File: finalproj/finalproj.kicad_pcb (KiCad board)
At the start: 2 copper layers, 99.2 x 99.6 mm, 44 parts, among them J10 MotorA Out, J11 MotorB Out, J5 Stepper_Motor_Controller, J7 LIDAR_Connector, J9 RPI_UART_Conn, U1 LM1085-12, U2 LM1085-12, U3 LM1085-5.0, U4 LM1085-3.3, U5 L298N

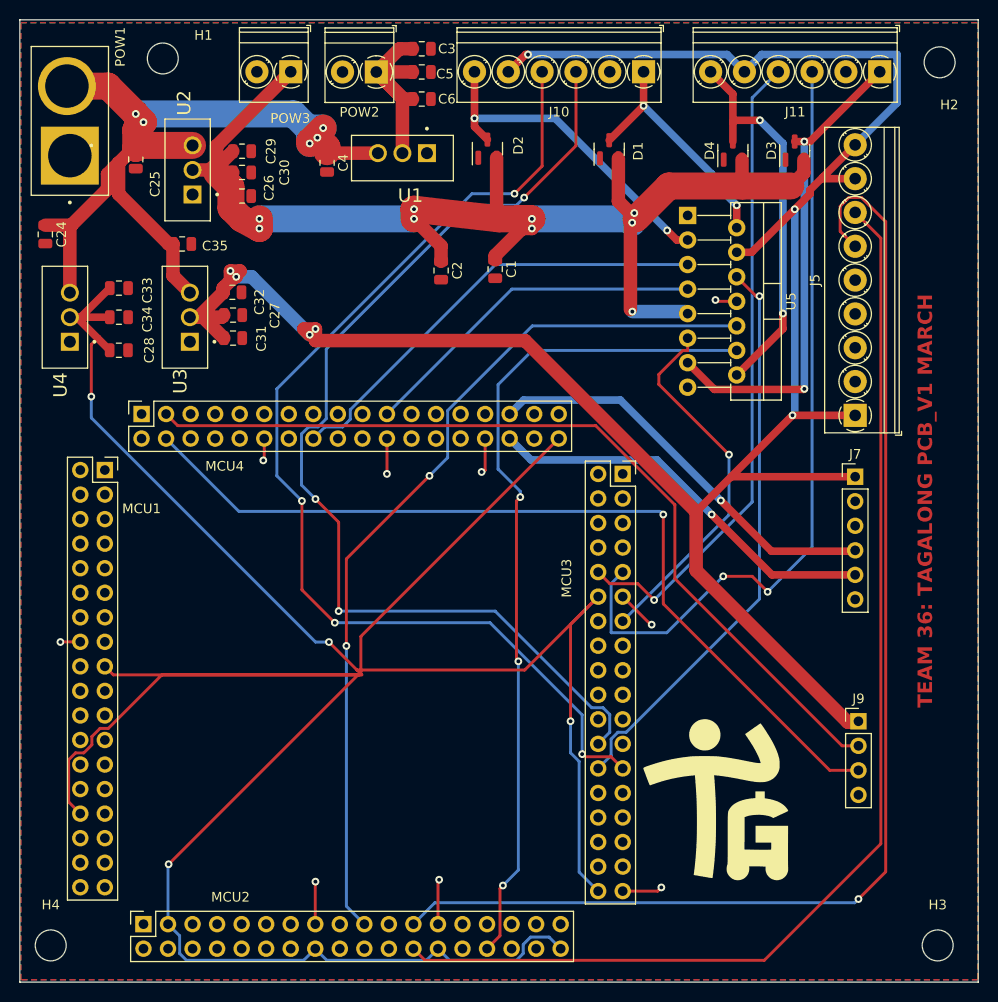
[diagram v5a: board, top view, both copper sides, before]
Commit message: Removed unused files (breakoutalt), fixed alignment issue of header pins
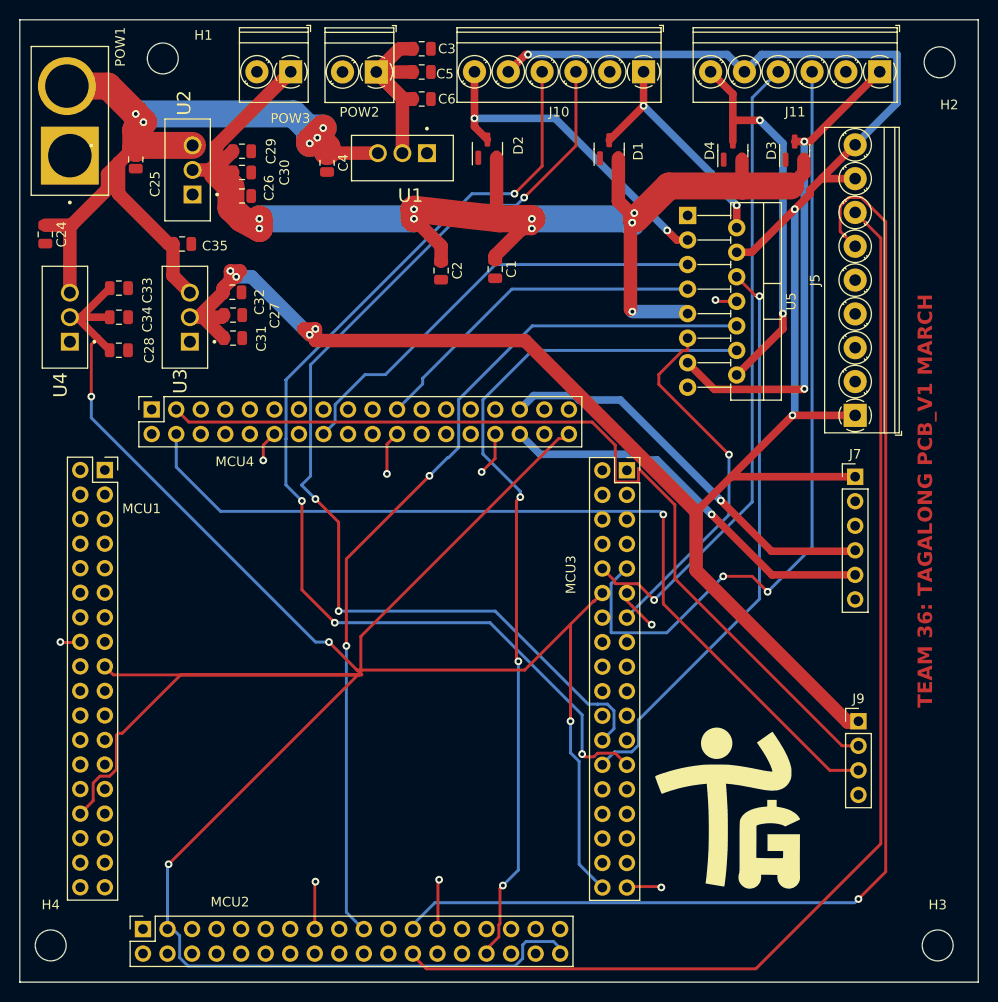
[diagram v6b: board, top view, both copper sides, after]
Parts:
- moved G*** 1.51 mm to (87.4, 94.5)
- moved MCU4 1.15 mm to (26.3, 52.7)
- moved MCU3 0.57 mm to (75.4, 59.0)
- moved MCU2 0.51 mm to (25.3, 106.5)
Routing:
- net VDD: track 304.4 -> 298.6 mm
- net VSS: track 31.6 -> 35.4 mm
- net RPI_UART_TX: track 90.4 -> 93.7 mm
- net MotorBIn2: track 87.1 -> 88.4 mm
- net STEP_PWM: track 120.3 -> 121.5 mm
- net RPI_UART_RX: track 91.3 -> 92.4 mm
- net MotorAIn2: track 36.5 -> 35.6 mm
- net LIDAR_SCL: track 42.9 -> 42.0 mm
- net MotorAIn1: track 46.8 -> 46.0 mm
- net LIDAR_SDA: track 41.6 -> 41.0 mm
- net MotorBPWM: track 38.4 -> 37.8 mm
- net MotorAPWM: track 59.5 -> 60.0 mm
- removed copper zone on B.Cu, net VSS
- removed copper zone on F.Cu, net VSS

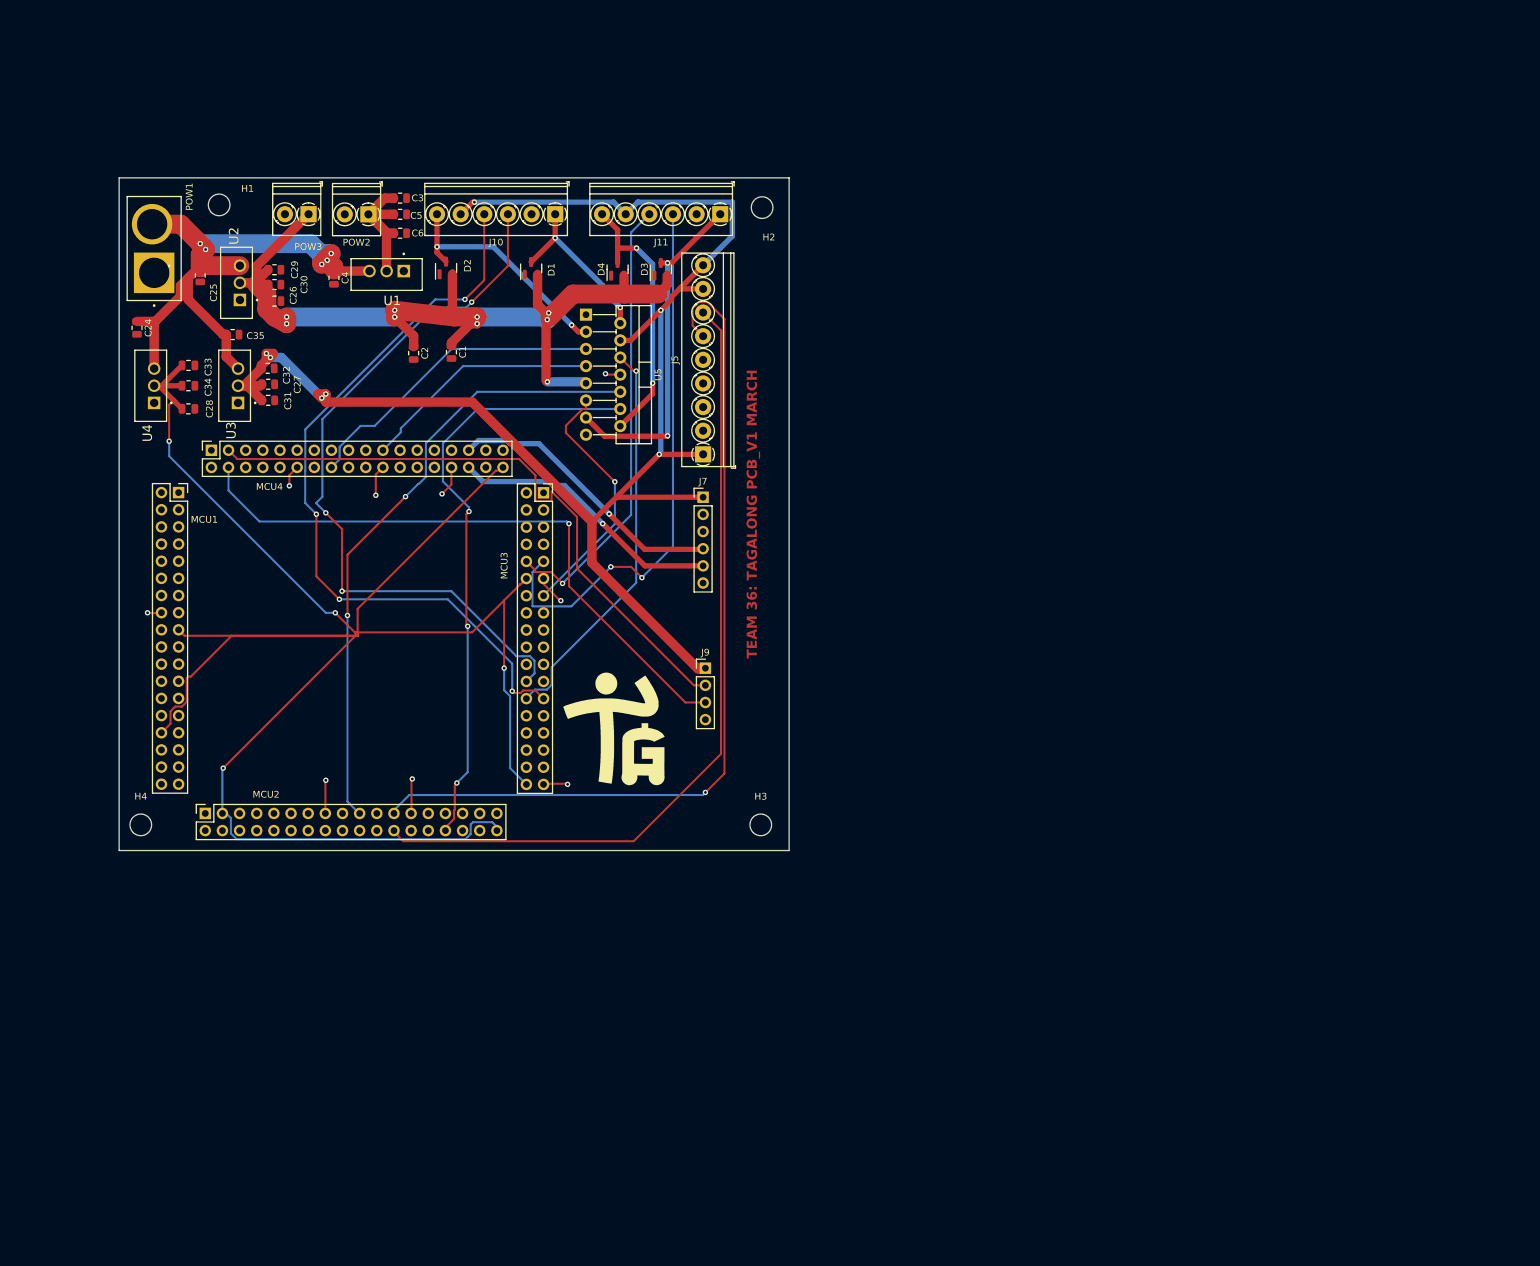
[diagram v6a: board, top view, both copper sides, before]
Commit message: fixed DRC erros on main board, had to revert breakout board headers to one sided since couldn't find lib
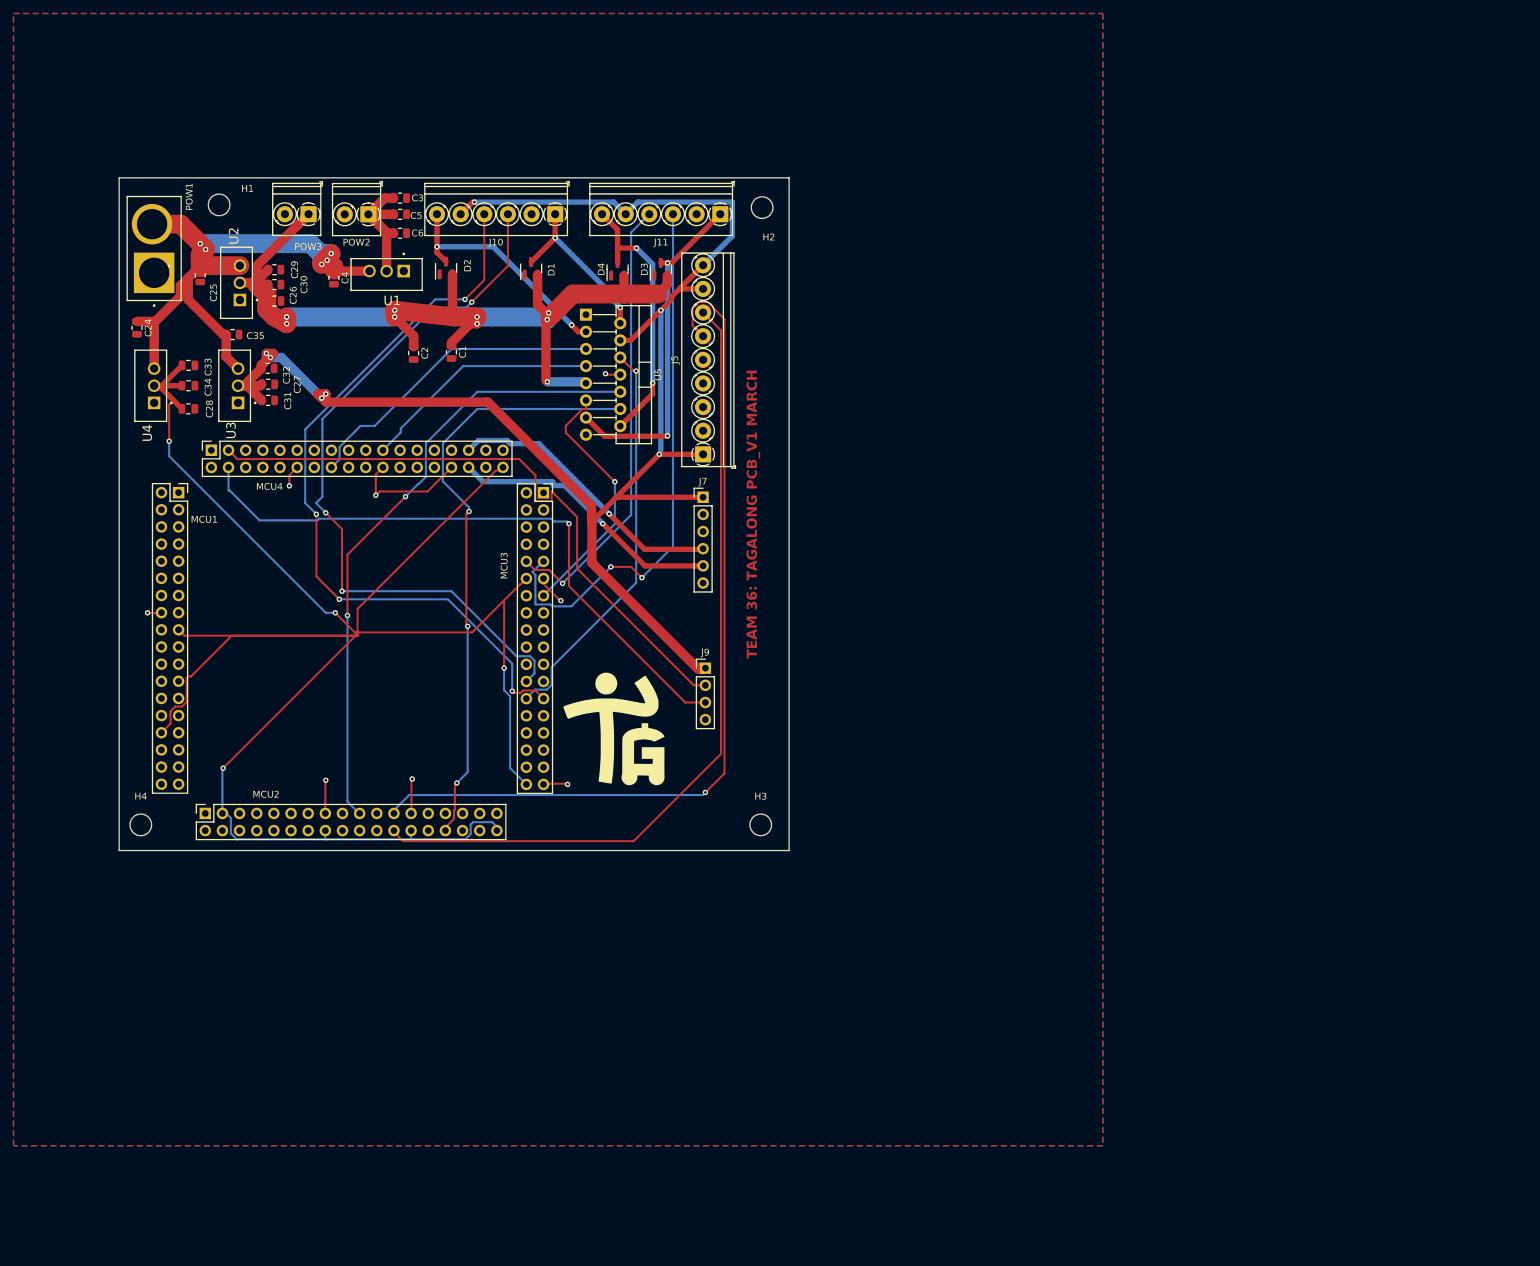
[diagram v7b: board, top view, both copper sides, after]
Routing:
- net VSS: track 35.4 -> 42.3 mm, vias 9 -> 8
- net VDD: track 298.6 -> 301.2 mm
- net +5V: track 236.0 -> 237.4 mm
- net STEP_PWM: track 121.5 -> 120.7 mm
- added copper zone on B.Cu, net VSS
- added copper zone on F.Cu, net VSS

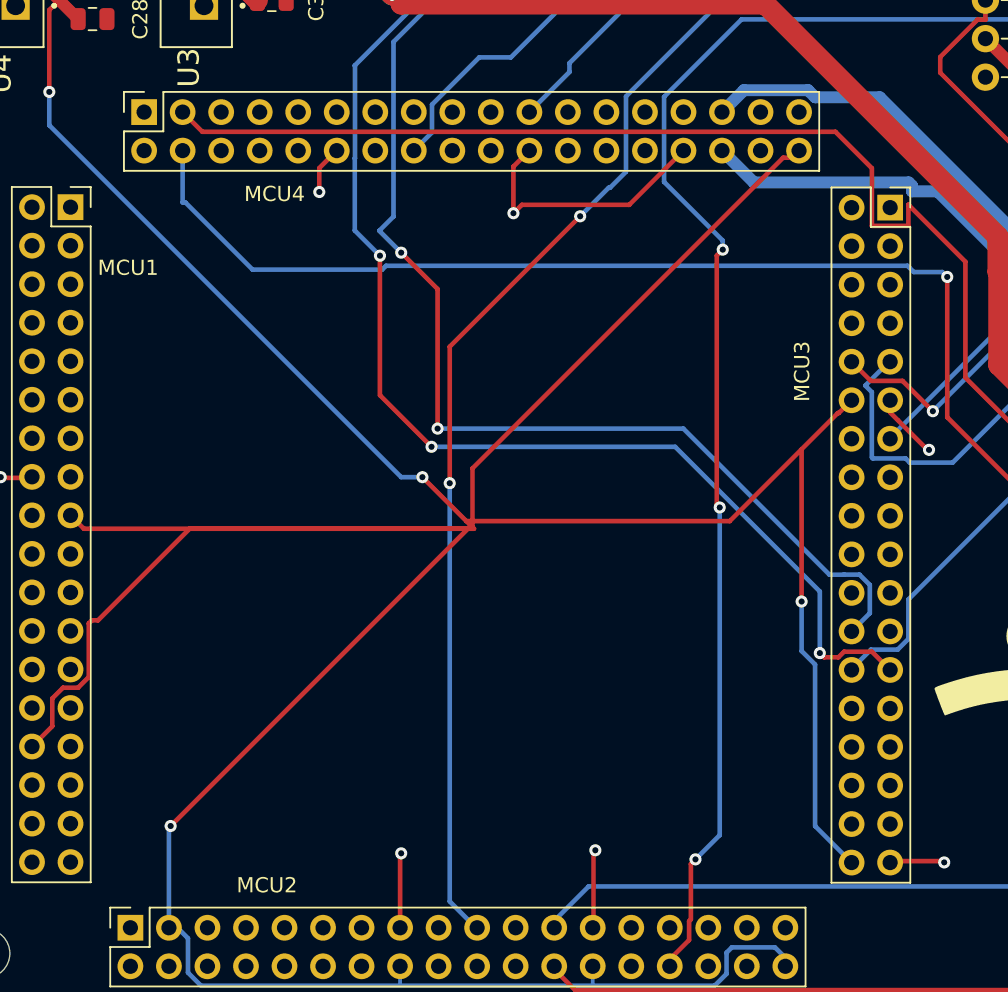
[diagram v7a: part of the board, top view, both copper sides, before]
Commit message: Verified proper orientation of mainboard sockets relative to breakoutboard pins
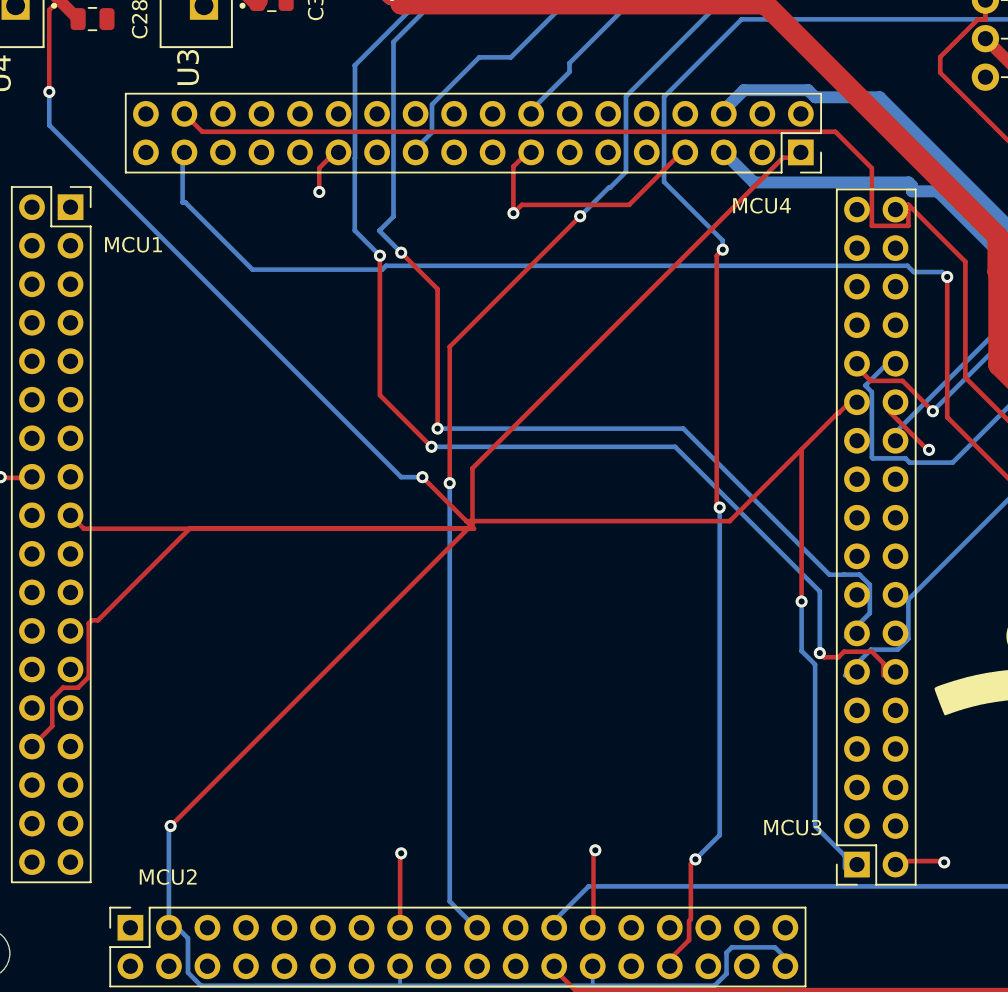
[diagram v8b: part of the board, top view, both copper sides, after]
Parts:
- moved MCU4 43.4 mm to (69.5, 55.4), turned to -90 degrees
- moved MCU3 43.4 mm to (73.2, 102.3), turned to 180 degrees
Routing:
- net VSS: track 42.3 -> 31.0 mm, vias 8 -> 5
- net MotorAPWM: track 60.0 -> 64.4 mm, vias 1 -> 2
- net unconnected-(MCU3-PB13-Pad74): track 0.00 -> 3.57 mm, vias 0 -> 1
- net unconnected-(MCU4-PB3-Pad133): track 0.00 -> 3.35 mm, vias 0 -> 1
